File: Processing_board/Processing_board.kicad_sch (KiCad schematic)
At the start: 26 parts, among them J1 Conn_01x08_Pin, J2 Conn_01x08_Pin, J3 Conn_01x06_Pin, J4 Conn_01x03_Pin, J5 Conn_01x03_Pin, J6 Conn_01x02_Pin, J7 Conn_01x02_Pin, SW1 TL3305BF100QG, SW2 TL3305BF100QG, U1 STM32WBA63CIU6

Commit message: more progress
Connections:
- net ADC/GPIO3 is gone; now on net LED: U1.19 (PB7)
- net LED: no longer U1.33 (PB15)
- net ADC_GPIO3: now reaches U1.47 (PA9)
- net ADC_GPIO2: now reaches U1.48 (PB14)
- net ADC/GPIO2: no longer names the net of U1.20 (PB6)
- no-connect marks 16 -> 15
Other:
- moved on the sheet: D1, R5

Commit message: more minor cleanup
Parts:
- added TP1: TestPoint, TestPoint:TestPoint_Pad_D1.0mm, symbol Connector:TestPoint
- added TP13: PN5260, PN5260:PN5260, symbol PN5260:5260
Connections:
- net SMPS_VSS is gone; now on net GND: U1.1 (VSSSMPS)
- net GND: now also TP13.1
- net OSC_IN: now also TP1.1
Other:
- note added: "32 MHz Oscillator (HSE)"
- note added: "QUESTIONS : 1) Each LED consumes ~10mA. Is that too much ? 2) How much current do I actually have available ? 3) I feel like my power switching/voltage adaptation circuit is shit"
- note removed: "Oscillator"
- note removed: "QUESTIONS : 1) Each LED consumes ~10mA. Is that too much ? 2) How much current do I actually have available ? 3) I feel like my power switching/voltage adaptation circuit is shit 4) Will the resistance added by the pin headers on each side of PCB_antenna fuck up the impedance ?"

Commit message: more cleanup
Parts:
- removed C1, C2: 100nF, Capacitor_SMD:C_0402_1005Metric, symbol Device:C_Small
- removed C3, C4: 10pF, Capacitor_SMD:C_0603_1608Metric, symbol Device:C_Small
- removed D1: IN_S42BT LED, LED_SMD:LED_0402_1005Metric, symbol Device:LED
- removed H1, H2: MountingHole, MountingHole:MountingHole_2.2mm_M2, symbol Mechanical:MountingHole
- removed J1, J2: Conn_01x08_Pin, Connector_PinHeader_2.54mm:PinHeader_1x08_P2.54mm_Vertical_SMD_Pin1Left, symbol Connector:Conn_01x08_Pin
- removed J3: Conn_01x06_Pin, Connector_PinHeader_2.54mm:PinHeader_1x06_P2.54mm_Vertical_SMD_Pin1Left, symbol Connector:Conn_01x06_Pin
- removed J4, J5: Conn_01x03_Pin, Connector_PinHeader_2.54mm:PinHeader_1x03_P2.54mm_Vertical_SMD_Pin1Left, symbol Connector:Conn_01x03_Pin
- removed J6, J7: Conn_01x02_Pin, Connector_PinHeader_2.54mm:PinHeader_1x02_P2.54mm_Vertical_SMD_Pin1Left, symbol Connector:Conn_01x02_Pin
- removed R1, R2, R3, R4, R5: 100R, Resistor_SMD:R_0402_1005Metric, symbol Device:R_Small
- removed R6, R8: 100R, Resistor_SMD:R_0402_1005Metric, symbol Device:R
- removed R7: 10k, Resistor_SMD:R_0402_1005Metric, symbol Device:R
- removed SW1, SW2: TL3305BF100QG, TL3305BF100QG:TL3305BF160QG, symbol TL3305BF100QG:TL3305BF100QG
- removed TP1: TestPoint, TestPoint:TestPoint_Pad_D1.0mm, symbol Connector:TestPoint
- removed TP13: PN5260, PN5260:PN5260, symbol PN5260:5260
- removed U1: STM32WBA63CIU6, SMT32WBA63:UFQFPN-48_STM, symbol STM32WBA63CI:STM32WBA63CIU6
- removed XTAL1: CX2016DB32000D0FLJCC, CX2016DB32000D0FLJCC:xtal4_CX2016DB_AVX, symbol CX2016DB32000D0FLJCC:CX2016DB32000D0FLJCC
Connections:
- no-connect marks 15 -> 0
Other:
- removed sheet ADC
- removed sheet Power switching and voltage adaptation
- removed sheet RF circuitry & antennas
- removed sheet STM32_power_supply_scheme
- removed sheet USB-C circuit
- added sheet Block_Diagram (Block_Diagram.kicad_sch)
- added sheet Schematic (Schematic.kicad_sch)
- note added: "CLICK HERE FOR SCHEMATIC"
- note removed: "32 MHz Oscillator (HSE)"
- note removed: "ADC is linked to STM32 on SPI_3 MCP2220 is linked to STM32 on USART1"
- note removed: "CL = (Cl1*Cl2)/(Cl1+Cl2) + Cs CL = crystal's load capacitance = 8 Cs = stray capacitance (assumed 3pF) Cl1= Cl2 = pierce oscillator's capacitors Cl"
- note removed: "Cl = 2(CL-Cs) = 2(8-3) = 10 pF"
- note removed: "Connector for the powerboard line (battery 5V)"
- note removed: "EMG boards power"
- note removed: "Flash button"
- note removed: "GND"
- note removed: "NRST"
- note removed: "Push and maintain button BEFORE board power-up (or reset) to enter flashing mode"
- note removed: "QUESTIONS : 1) Each LED consumes ~10mA. Is that too much ? 2) How much current do I actually have available ? 3) I feel like my power switching/voltage adaptation circuit is shit"
- note removed: "R12 and C3 in combo with the pulldown resistor form a low-pass filter for button debouncing"
- note removed: "RX"
- note removed: "Reset button"
- note removed: "SPI3_MISO"
- note removed: "SPI3_MOSI"
- note removed: "SPI3_SCK"
- note removed: "SWCLK"
- note removed: "SWD traces"
- note removed: "SWD/JTAG"
- note removed: "SWD/JTAG is for debug and flashing (apparently UART can also be used for flashing ?) IO & CLK are important, Trace is for additional debug capability or can be GPIO if needed"
- note removed: "SWDIO"
- note removed: "TX"
- note removed: "The 100R resistor is ESD protection apparently"
- note removed: "Traces"
- note removed: "USART2 RX"
- note removed: "USART3 RX"
- note removed: "USART3_TX"
- note removed: "USART_1 RX"
- note removed: "USART_1 TX"
- note removed: "USART_2"
- note removed: "USART_2 TX"
- note removed: "USART_3"
- note removed: "VCC"

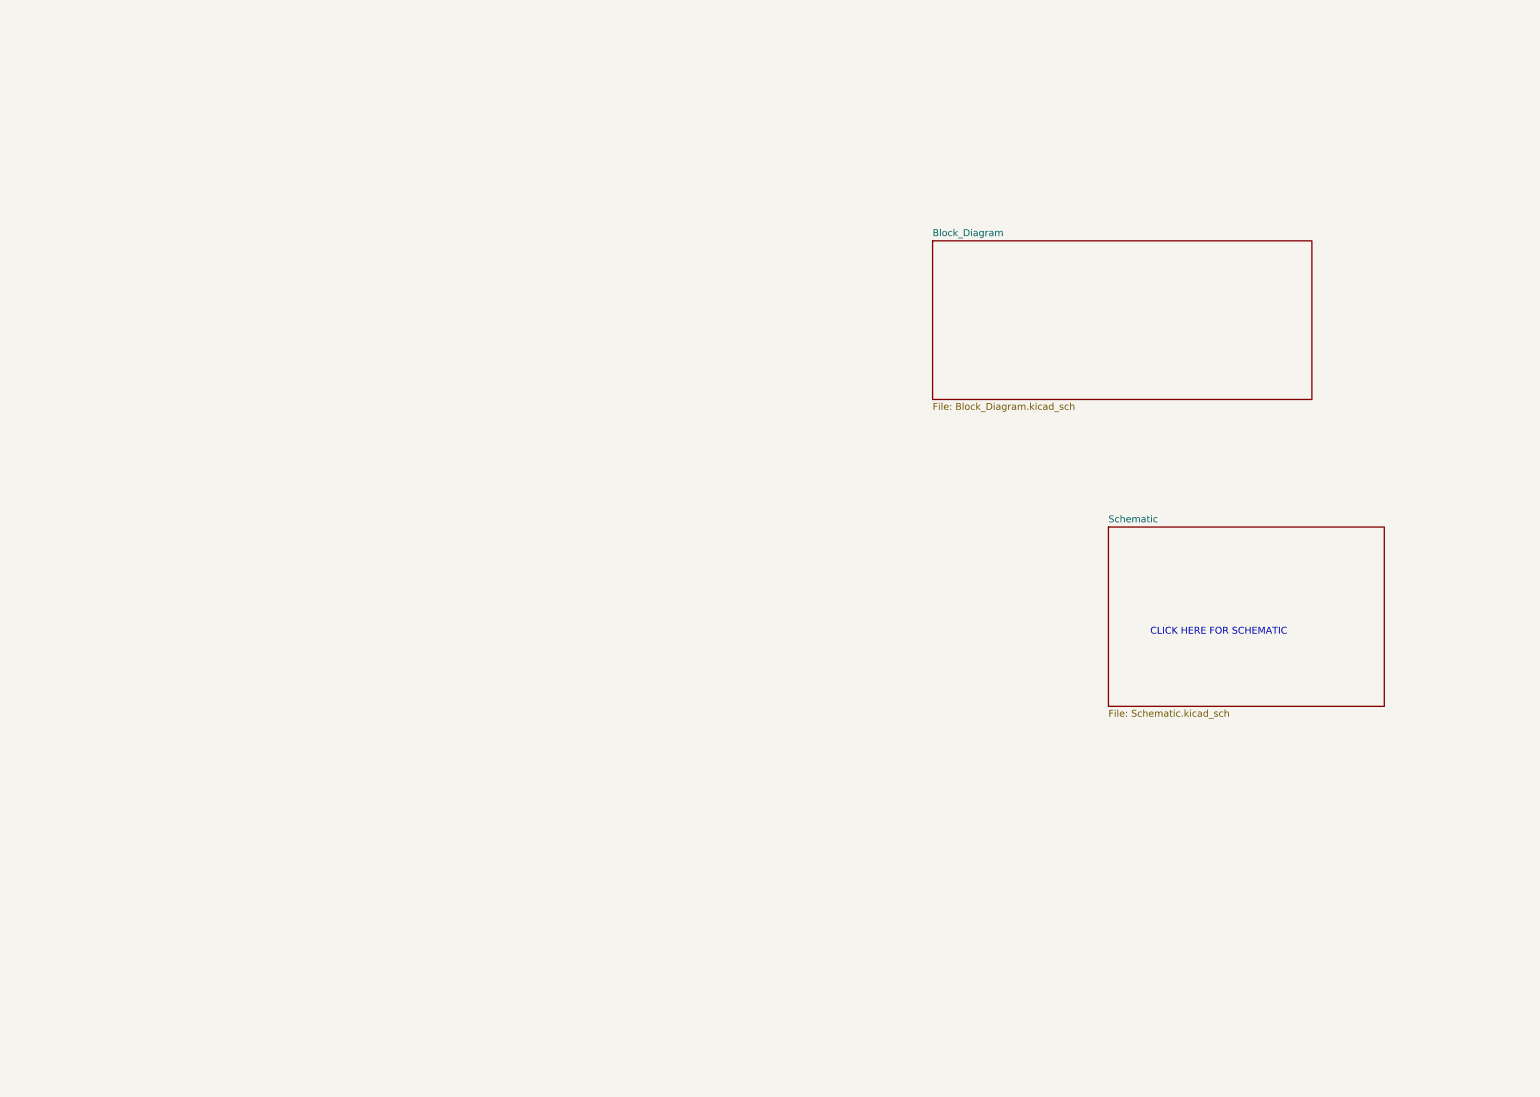
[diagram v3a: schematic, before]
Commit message: had to rename all components on the PCB to match the schematic
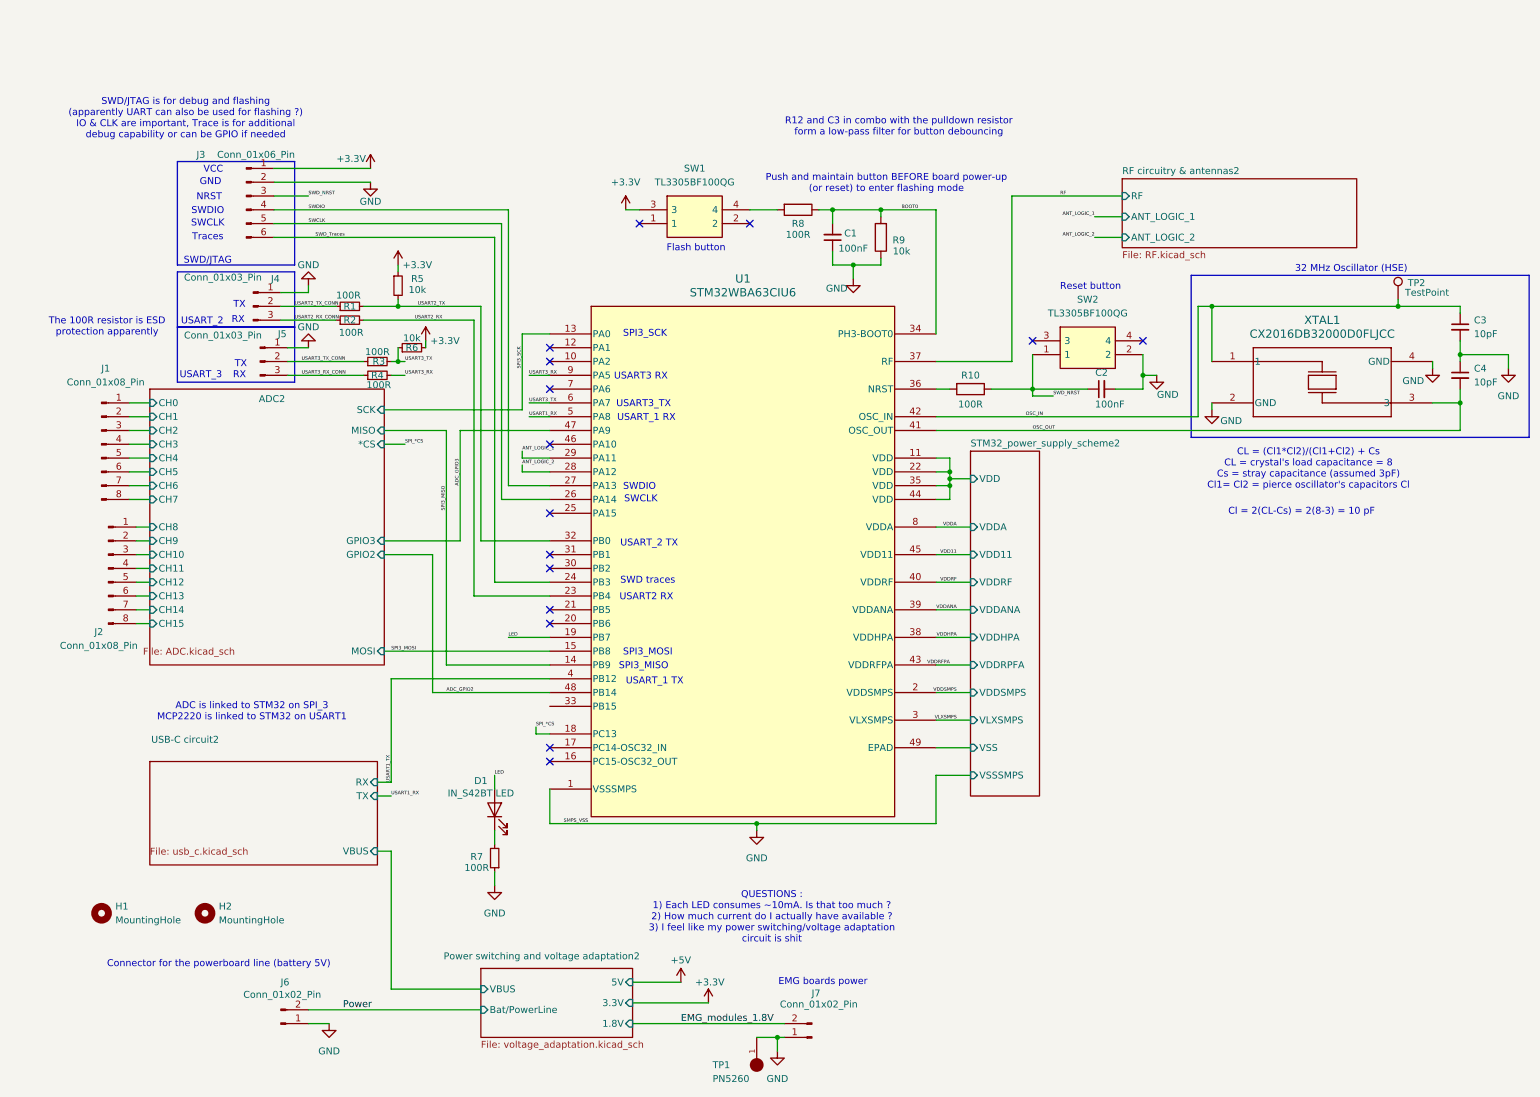
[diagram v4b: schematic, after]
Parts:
- added C1, C2: 100nF, Capacitor_SMD:C_0402_1005Metric, symbol Device:C_Small
- added C3, C4: 10pF, Capacitor_SMD:C_0603_1608Metric, symbol Device:C_Small
- added D1: IN_S42BT LED, LED_SMD:LED_0402_1005Metric, symbol Device:LED
- added H1, H2: MountingHole, MountingHole:MountingHole_2.2mm_M2, symbol Mechanical:MountingHole
- added J1, J2: Conn_01x08_Pin, Connector_PinHeader_2.54mm:PinHeader_1x08_P2.54mm_Vertical_SMD_Pin1Left, symbol Connector:Conn_01x08_Pin
- added J3: Conn_01x06_Pin, Connector_PinHeader_2.54mm:PinHeader_1x06_P2.54mm_Vertical_SMD_Pin1Left, symbol Connector:Conn_01x06_Pin
- added J4, J5: Conn_01x03_Pin, Connector_PinHeader_2.54mm:PinHeader_1x03_P2.54mm_Vertical_SMD_Pin1Left, symbol Connector:Conn_01x03_Pin
- added J6, J7: Conn_01x02_Pin, Connector_PinHeader_2.54mm:PinHeader_1x02_P2.54mm_Vertical_SMD_Pin1Left, symbol Connector:Conn_01x02_Pin
- added R1, R2, R3, R4, R7: 100R, Resistor_SMD:R_0402_1005Metric, symbol Device:R_Small
- added R10, R8: 100R, Resistor_SMD:R_0402_1005Metric, symbol Device:R
- added R5, R6: 10k, Resistor_SMD:R_0402_1005Metric, symbol Device:R_Small
- added R9: 10k, Resistor_SMD:R_0402_1005Metric, symbol Device:R
- added SW1, SW2: TL3305BF100QG, TL3305BF100QG:TL3305BF160QG, symbol TL3305BF100QG:TL3305BF100QG
- added TP1: PN5260, PN5260:PN5260, symbol PN5260:5260
- added TP2: TestPoint, TestPoint:TestPoint_Pad_D1.0mm, symbol Connector:TestPoint
- added U1: STM32WBA63CIU6, SMT32WBA63:UFQFPN-48_STM, symbol STM32WBA63CI:STM32WBA63CIU6
- added XTAL1: CX2016DB32000D0FLJCC, CX2016DB32000D0FLJCC:xtal4_CX2016DB_AVX, symbol CX2016DB32000D0FLJCC:CX2016DB32000D0FLJCC
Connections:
- new net: R10.2, U1.36 (NRST)
- new net: R8.2, SW1.4
- new net: D1.1 (K), R7.2
- new net +3.3V: J3.1 (Pin_1), R5.1, R6.2, SW1.3
- new net ADC2/CH0: J1.1 (Pin_1)
- new net ADC2/CH1: J1.2 (Pin_2)
- new net ADC2/CH10: J2.3 (Pin_3)
- new net ADC2/CH11: J2.4 (Pin_4)
- new net ADC2/CH12: J2.5 (Pin_5)
- new net ADC2/CH13: J2.6 (Pin_6)
- new net ADC2/CH14: J2.7 (Pin_7)
- new net ADC2/CH15: J2.8 (Pin_8)
- new net ADC2/CH2: J1.3 (Pin_3)
- new net ADC2/CH3: J1.4 (Pin_4)
- new net ADC2/CH4: J1.5 (Pin_5)
- new net ADC2/CH5: J1.6 (Pin_6)
- new net ADC2/CH6: J1.7 (Pin_7)
- new net ADC2/CH7: J1.8 (Pin_8)
- new net ADC2/CH8: J2.1 (Pin_1)
- new net ADC2/CH9: J2.2 (Pin_2)
- new net ADC_GPIO2: U1.48 (PB14)
- new net ADC_GPIO3: U1.47 (PA9)
- new net ANT_LOGIC_1: U1.29 (PA11)
- new net ANT_LOGIC_2: U1.28 (PA12)
- new net BOOT0: C1.2, R8.1, R9.2, U1.34 (PH3-BOOT0)
- new net EMG_modules_1.8V: J7.2 (Pin_2)
- new net GND: C1.1, C2.2, C3.2, C4.1, J3.2 (Pin_2), J4.1 (Pin_1), J5.1 (Pin_1), J6.1 (Pin_1), J7.1 (Pin_1), R7.1, R9.1, SW2.2, TP1.1, U1.1 (VSSSMPS), XTAL1.2 (GND), XTAL1.4 (GND)
- new net LED: D1.2 (A), U1.19 (PB7)
- new net OSC_IN: C3.1, TP2.1, U1.42 (OSC_IN), XTAL1.1
- new net OSC_OUT: C4.2, U1.41 (OSC_OUT), XTAL1.3
- new net Power: J6.2 (Pin_2)
- new net RF: U1.37 (RF)
- new net SPI3_MISO: U1.14 (PB9)
- new net SPI3_MOSI: U1.15 (PB8)
- new net SPI3_SCK: U1.13 (PA0)
- new net SPI_*CS: U1.18 (PC13)
- new net STM32_power_supply_scheme2/VDD: U1.11 (VDD), U1.22 (VDD), U1.35 (VDD), U1.44 (VDD)
- new net STM32_power_supply_scheme2/VSS: U1.49 (EPAD)
- new net SWCLK: J3.5 (Pin_5), U1.26 (PA14)
- new net SWDIO: J3.4 (Pin_4), U1.27 (PA13)
- new net SWD_NRST: C2.1, J3.3 (Pin_3), R10.1, SW2.1
- new net SWD_Traces: J3.6 (Pin_6), U1.24 (PB3)
- new net USART1_RX: U1.5 (PA8)
- new net USART1_TX: U1.4 (PB12)
- new net USART2_RX: R2.2, U1.23 (PB4)
- new net USART2_RX_CONN: J4.3 (Pin_3), R2.1
- new net USART2_TX: R1.2, R5.2, U1.32 (PB0)
- new net USART2_TX_CONN: J4.2 (Pin_2), R1.1
- new net USART3_RX: R4.2, U1.9 (PA5)
- new net USART3_RX_CONN: J5.3 (Pin_3), R4.1
- new net USART3_TX: R3.2, R6.1, U1.6 (PA7)
- new net USART3_TX_CONN: J5.2 (Pin_2), R3.1
- new net VDD11: U1.45 (VDD11)
- new net VDDA: U1.8 (VDDA)
- new net VDDANA: U1.39 (VDDANA)
- new net VDDHPA: U1.38 (VDDHPA)
- new net VDDRF: U1.40 (VDDRF)
- new net VDDRFPA: U1.43 (VDDRFPA)
- new net VDDSMPS: U1.2 (VDDSMPS)
- new net VLXSMPS: U1.3 (VLXSMPS)
- no-connect marks 0 -> 15
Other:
- removed sheet Block_Diagram
- removed sheet Schematic
- added sheet ADC2 (ADC.kicad_sch)
- added sheet Power switching and voltage adaptation2 (voltage_adaptation.kicad_sch)
- added sheet RF circuitry & antennas2 (RF.kicad_sch)
- added sheet STM32_power_supply_scheme2 (STM32_power_supply_scheme.kicad_sch)
- added sheet USB-C circuit2 (usb_c.kicad_sch)
- note added: "32 MHz Oscillator (HSE)"
- note added: "ADC is linked to STM32 on SPI_3 MCP2220 is linked to STM32 on USART1"
- note added: "CL = (Cl1*Cl2)/(Cl1+Cl2) + Cs CL = crystal's load capacitance = 8 Cs = stray capacitance (assumed 3pF) Cl1= Cl2 = pierce oscillator's capacitors Cl"
- note added: "Cl = 2(CL-Cs) = 2(8-3) = 10 pF"
- note added: "Connector for the powerboard line (battery 5V)"
- note added: "EMG boards power"
- note added: "Flash button"
- note added: "GND"
- note added: "NRST"
- note added: "Push and maintain button BEFORE board power-up (or reset) to enter flashing mode"
- note added: "QUESTIONS : 1) Each LED consumes ~10mA. Is that too much ? 2) How much current do I actually have available ? 3) I feel like my power switching/voltage adaptation circuit is shit"
- note added: "R12 and C3 in combo with the pulldown resistor form a low-pass filter for button debouncing"
- note added: "RX"
- note added: "Reset button"
- note added: "SPI3_MISO"
- note added: "SPI3_MOSI"
- note added: "SPI3_SCK"
- note added: "SWCLK"
- note added: "SWD traces"
- note added: "SWD/JTAG"
- note added: "SWD/JTAG is for debug and flashing (apparently UART can also be used for flashing ?) IO & CLK are important, Trace is for additional debug capability or can be GPIO if needed"
- note added: "SWDIO"
- note added: "TX"
- note added: "The 100R resistor is ESD protection apparently"
- note added: "Traces"
- note added: "USART2 RX"
- note added: "USART3 RX"
- note added: "USART3_TX"
- note added: "USART_1 RX"
- note added: "USART_1 TX"
- note added: "USART_2"
- note added: "USART_2 TX"
- note added: "USART_3"
- note added: "VCC"
- note removed: "CLICK HERE FOR SCHEMATIC"

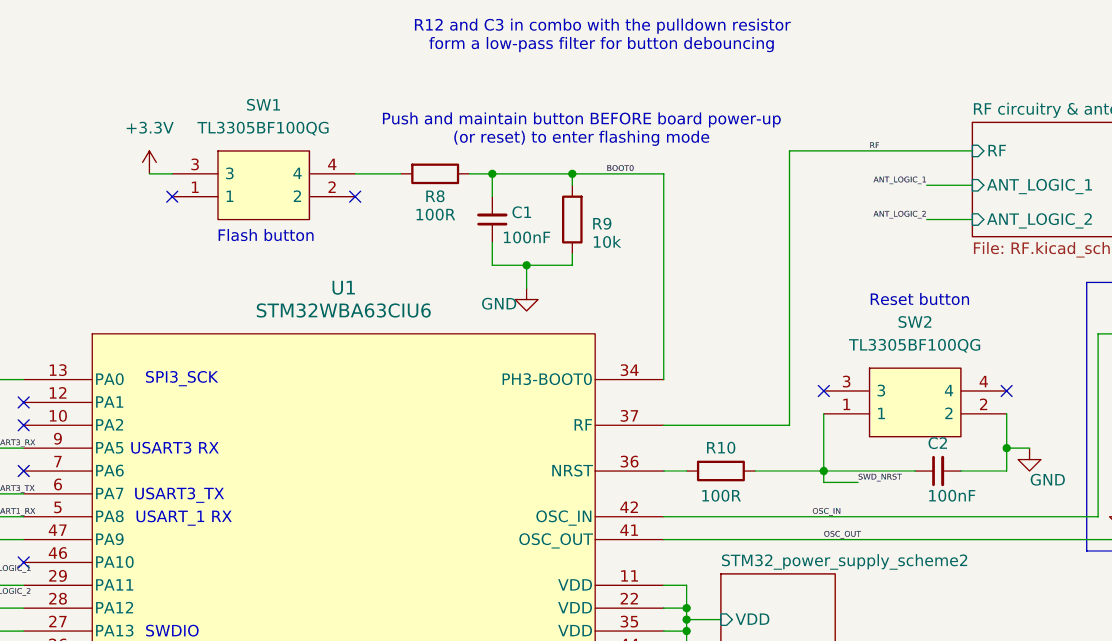
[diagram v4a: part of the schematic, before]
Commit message: created BOM, deleted useless folder Components and renamed CAD_Models to Parts
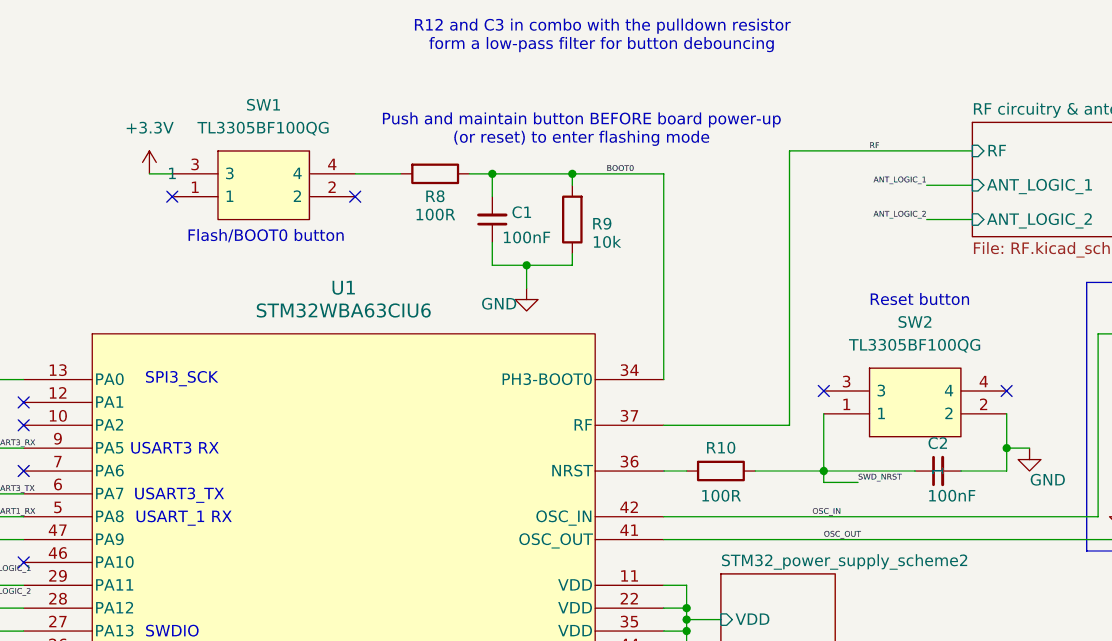
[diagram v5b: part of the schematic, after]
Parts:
- C1, C2: Link (none) -> https://www.mouser.ch/ProductDetail/Samsung-Electro-Mechani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; MANUFACTURER (none) -> Samsung Electro-Mechanics; Manufacturer_Part_Number (none) -> CL05B104KP5VPNC; Panier (none) -> 1
- C3, C4: Link (none) -> https://www.mouser.ch/ProductDetail/KYOCERA-AVX/0603ZC100KA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; MANUFACTURER (none) -> KYOCERA AVX; Manufacturer_Part_Number (none) -> 0603ZC100KAT2A; Panier (none) -> 1
- D1: Link (none) -> https://www.mouser.ch/ProductDetail/Inolux/IN-S42BT5G?qs=mA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; MANUFACTURER (none) -> Inolux; Manufacturer_Part_Number (none) -> IN-S42BT5G; Panier (none) -> 1
- R1, R10, R2, R3, R4, R7, R8: Link (none) -> https://www.mouser.ch/ProductDetail/KOA-Speer/RK73B1ETTPD10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; MANUFACTURER (none) -> KOA Speer; Manufacturer_Part_Number (none) -> RK73B1ETTPD101J; Panier (none) -> 1
- R5, R6, R9: Link (none) -> https://www.mouser.ch/ProductDetail/Wurth-Elektronik/560112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; MANUFACTURER (none) -> Wurth Elektronik; Manufacturer_Part_Number (none) -> 560112110020; Panier (none) -> 1
- SW1, SW2: Link (none) -> https://www.mouser.ch/ProductDetail/E-Switch/TL3305BF100QG?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; MANUFACTURER (none) -> E-Switch; Panier (none) -> 1
- TP1: Link (none) -> https://www.mouser.ch/ProductDetail/Keystone-Electronics/52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; Manufacturer_Part_Number (none) -> 5260; Panier (none) -> 1
- U1: Link (none) -> https://www.mouser.ch/ProductDetail/STMicroelectronics/STM3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; MANUFACTURER (none) -> STMicroelectronics; Manufacturer_Part_Number (none) -> STM32WBA63CIU6; déjà (none) -> 1
- XTAL1: Link (none) -> https://www.mouser.ch/ProductDetail/KYOCERA-AVX/CX2016DB320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; MANUFACTURER (none) -> KYOCERA AVX; Manufacturer_Part_Number (none) -> CX2016DB32000D0FLJCC; déjà (none) -> 1
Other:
- note added: "Flash/BOOT0 button"
- note removed: "Flash button"
